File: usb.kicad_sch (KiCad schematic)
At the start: 1 part, among them U1 MIMX8MN5DVPIZAA

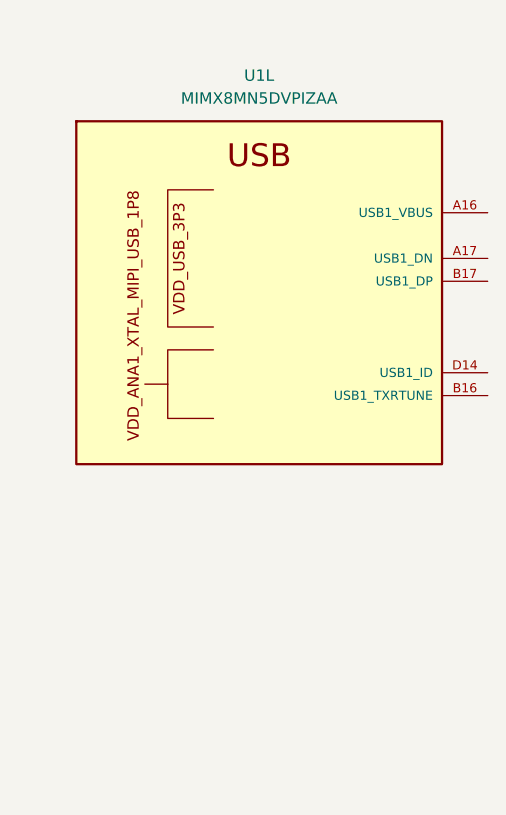
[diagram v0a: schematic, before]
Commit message: move to i.MX8M Mini
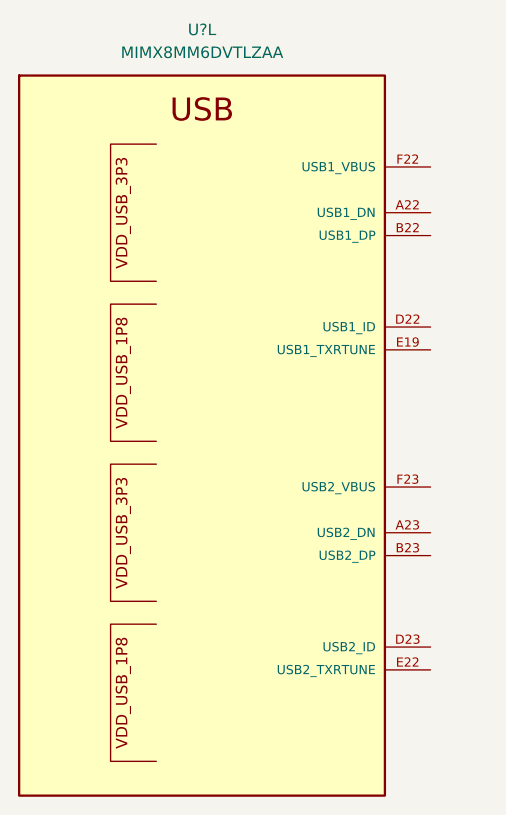
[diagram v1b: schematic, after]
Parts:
- removed U1: MIMX8MN5DVPIZAA, qsbc:SOT1967-1, symbol qsbc:MIMX8MN5DVPIZAA
- added U?: MIMX8MM6DVTLZAA, qsbc:SOT1967-1, symbol qsbc:MIMX8MM6DVTLZAA

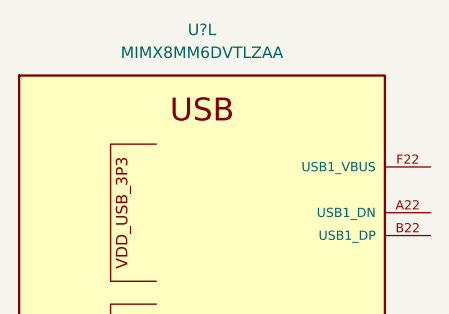
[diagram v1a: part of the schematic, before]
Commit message: ddr sch done
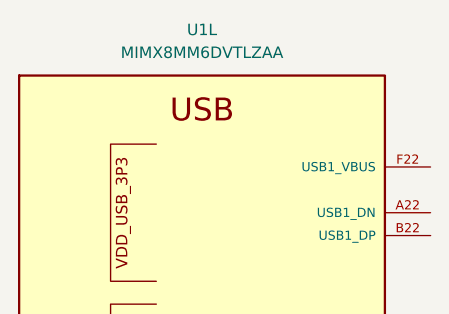
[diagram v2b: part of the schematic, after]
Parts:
- gave numbers to parts that had none: 1
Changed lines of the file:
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@@
   (symbol (lib_id "qsbc:MIMX8MM6DVTLZAA") (at 140.97 62.23 0) (unit 12)
     (in_bom yes) (on_board yes) (fields_autoplaced)
-    (property "Reference" "U?" (id 0) (at 140.97 43.18 0))
+    (property "Reference" "U1" (id 0) (at 140.97 43.18 0))
     (property "Value" "MIMX8MM6DVTLZAA" (id 1) (at 140.97 45.72 0))
     (property "Footprint" "qsbc:SOT1967-1" (id 2) (at 144.78 252.73 0)

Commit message: misc work, usb sch done
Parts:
- added C50, C51, C53, C? (x5): 0.1uF, Capacitor_SMD:C_0402_1005Metric, symbol Device:C
- added C52, C?: 1nF, Capacitor_SMD:C_0603_1608Metric, symbol Device:C
- added C54, C?: 10uF, Capacitor_SMD:C_0603_1608Metric, symbol Device:C
- added C? (x2): 0.22uF, Capacitor_SMD:C_0402_1005Metric, symbol Device:C
- added C?: 1uF, Capacitor_SMD:C_0402_1005Metric, symbol Device:C
- added D1: LED YELLOW, LED_SMD:LED_0402_1005Metric, symbol Device:LED
- added FB1, FB? (x3): FerriteBead, Resistor_SMD:R_0603_1608Metric, symbol Device:FerriteBead
- added J1, J3, J? (x2): USB_C_Receptacle_USB2.0, Connector_USB:USB_C_Receptacle_HRO_TYPE-C-31-M-12, symbol Connector:USB_C_Receptacle_USB2.0
- added R12, R13, R14, R? (x4): 100K, Resistor_SMD:R_0402_1005Metric, symbol Device:R
- added R15, R16, R? (x2): 0R, symbol Device:R
- added R17, R?: 30K, Resistor_SMD:R_0402_1005Metric, symbol Device:R
- added R18, R?: 1M, Resistor_SMD:R_0402_1005Metric, symbol Device:R
- added R? (x2): 30K, Resistor_SMD:R_0201_0603Metric, symbol Device:R
- added R? (x4): 0R, Resistor_SMD:R_0402_1005Metric, symbol Device:R
- added R?: 2.2K, Resistor_SMD:R_0402_1005Metric, symbol Device:R
- added R? (x4): 5.1K, Resistor_SMD:R_0402_1005Metric, symbol Device:R
- added R? (x2): 200R, Resistor_SMD:R_0201_0603Metric, symbol Device:R
- added R?: 10K, Resistor_SMD:R_0402_1005Metric, symbol Device:R
- added R?: 10m, Resistor_SMD:R_1206_3216Metric, symbol Device:R
- added TP?: TestPoint, TestPoint:TestPoint_Pad_D1.5mm, symbol Connector:TestPoint
- added U10, U?: TUSB320LI, Package_DFN_QFN:Texas_X2QFN-12_1.6x1.6mm_P0.4mm, symbol Interface_USB:TUSB320
- added U12, U4, U?: TPD4EUSB30, Package_SON:USON-10_2.5x1.0mm_P0.5mm, symbol qsbc:TPD4EUSB30
- added U19, U?: NX5P3363, Package_CSP:WLCSP-16_2.225x2.17mm_P0.5mm, symbol qsbc:NX5P3363
- added U20, U? (x3): D5V0H1B2LP, symbol qsbc:D5V0H1B2LP
- added U8, U?: 74LVC1G04, Package_TO_SOT_SMD:SOT-23-5, symbol 74xGxx:74LVC1G04
- added U?: INA231, qsbc:DSBGA-12, symbol qsbc:INA231
- added U?: CH343P, Package_DFN_QFN:QFN-16-1EP_3x3mm_P0.5mm_EP1.45x1.45mm_ThermalVias, symbol qsbc:CH343P
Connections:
- net USB1_DN: now reaches U1.A22 (USB1_DN)
- net USB1_DN: now also J?.A7 (D-), J?.B7 (D-), U?.4 (D2+), U?.7
- net USB2_DN: now reaches U1.A23 (USB2_DN)
- net USB2_DN: now also J3.A7 (D-), J3.B7 (D-), U12.4 (D2+), U12.7
- net USB1_DP: now reaches U1.B22 (USB1_DP)
- net USB1_DP: now also J?.A6 (D+), J?.B6 (D+), U?.5 (D2-), U?.6
- net USB2_DP: now reaches U1.B23 (USB2_DP)
- net USB2_DP: now also J3.A6 (D+), J3.B6 (D+), U12.5 (D2-), U12.6
- net USB1_ID: now reaches U1.D22 (USB1_ID)
- net USB1_ID: now also R?.2, U?.2, U?.9 (ID)
- net USB2_ID: now reaches U1.D23 (USB2_ID)
- net USB2_ID: now also R12.2, U10.9 (ID), U8.2
- net at U1.E19 (USB1_TXRTUNE): now also R?.1
- net at U1.E22 (USB2_TXRTUNE): now also R?.1
- net at U1.F22 (USB1_VBUS): now also R?.1
- net at U1.F23 (USB2_VBUS): now also R?.1
- new net: R?.1, U?.4
- new net: C?.1, U?.D4 (CAP)
- new net: FB?.1, J?.S1 (SHIELD) (x2)
- new net: R18.1, U10.4 (VBUS_DET)
- new net: FB1.1, J3.S1 (SHIELD)
- new net: R?.2, U?.13 (UART_RTS)
- new net: D1.2 (A), R?.1
- new net: R?.2, U?.12 (UART_DTR/TNOW)
- new net: R?.2, U?.15 (UART_CTS)
- new net: R?.2, U?.4 (UART_TXD)
- new net: R?.1, U?.4 (VBUS_DET)
- new net: R?.1, U?.A3 (ILIM)
- new net: R16.1, U8.4
- new net: C52.1, U19.D4 (CAP)
- new net: R?.1, U?.10 (~{ACT})
- new net: R?.2, U?.5 (UART_RXD)
- new net: R17.1, U19.A3 (ILIM)
- new net: U4.1 (D1+), U4.10
- new net: U4.2 (D1-), U4.9
- new net: FB?.1, J1.S1 (SHIELD)
- new net GND: C50.2, C51.2, C52.2, C53.2, C54.2, C?.2, C?.2, C?.2, C?.2, C?.2, C?.2, C?.2, C?.2, C?.2, C?.2, D1.1 (K), FB1.2, FB?.2, FB?.2, FB?.2, J1.A1 (GND), J1.A12 (GND), J1.B1 (GND), J1.B12 (GND), J3.A1 (GND), J3.A12 (GND), J3.B1 (GND), J3.B12 (GND), J?.A1 (GND), J?.A1 (GND), J?.A12 (GND), J?.A12 (GND), J?.B1 (GND), J?.B1 (GND), J?.B12 (GND), J?.B12 (GND), R17.2, R?.2, R?.2, R?.2, R?.2, R?.2, R?.2, R?.2, R?.2, U10.10 (GND), U10.11 (~{EN}), U10.5 (ADDR), U12.3 (GND), U12.8 (GND), U19.B3 (GND), U19.C3 (GND), U19.D3 (GND), U20.2, U4.3 (GND), U4.8 (GND), U8.3 (GND), U?.1 (VDDIO), U?.10 (GND), U?.11 (~{EN}), U?.2, U?.2, U?.2, U?.2 (GND), U?.3 (GND), U?.3 (GND), U?.8 (GND), U?.B3 (A0), U?.B3 (GND), U?.C1 (GND), U?.C3 (A1), U?.C3 (GND), U?.D3 (GND)
- new net I2Cx_SCL: U10.8 (SCL/OUT2), U?.8 (SCL/OUT2), U?.A1 (SCL)
- new net I2Cx_SDA: U10.7 (SDA/OUT1), U?.7 (SDA/OUT1), U?.A2 (SDA)
- new net UART2_CTS: R?.1
- new net UART2_RTS: R?.1
- new net UART2_RXI: R?.1
- new net UART2_TXO: R?.1
- new net USB1_CC1: J?.A5 (CC1), U?.1 (CC1), U?.1 (D1+), U?.10
- new net USB1_CC2: J?.B5 (CC2), U?.2 (CC2), U?.2 (D1-), U?.9
- new net USB1_VBUS: C?.1, C?.1, J?.A4 (VBUS), J?.A9 (VBUS), J?.B4 (VBUS), J?.B9 (VBUS), R?.2, R?.2, U?.1, U?.C2 (VBUS), U?.D1 (VBUS), U?.D2 (VBUS)
- new net USB1_VBUS_EN: R?.1
- new net USB1_VBUS_EN_R: R?.2, R?.2, U?.B4 (EN)
- new net USB2_CC1: J3.A5 (CC1), U10.1 (CC1), U12.1 (D1+), U12.10
- new net USB2_CC2: J3.B5 (CC2), U10.2 (CC2), U12.2 (D1-), U12.9
- new net USB2_VBUS: C54.1, C?.1, J3.A4 (VBUS), J3.A9 (VBUS), J3.B4 (VBUS), J3.B9 (VBUS), R18.2, R?.2, U19.C2 (VBUS), U19.D1 (VBUS), U19.D2 (VBUS), U20.1
- new net USB2_VBUS_EN: R15.1
- new net USB2_VBUS_EN_R: R15.2, R16.2, U19.B4 (EN)
- new net USB3_CC1: J1.A5 (CC1), R?.1
- new net USB3_CC2: J1.B5 (CC2), R?.1
- new net USB3_DN: J1.A7 (D-), J1.B7 (D-), U4.5 (D2-), U4.6, U?.8 (USB_DN)
- new net USB3_DP: J1.A6 (D+), J1.B6 (D+), U4.4 (D2+), U4.7, U?.7 (USB_DP)
- new net USB3_VBUS: J1.A4 (VBUS), J1.A9 (VBUS), J1.B4 (VBUS), J1.B9 (VBUS), U?.1, U?.9 (USB_VBUS)
- new net USB4_CC1: J?.A5 (CC1), R?.1
- new net USB4_CC2: J?.B5 (CC2), R?.1
- new net USB4_VBUS: J?.A4 (VBUS), J?.A9 (VBUS), J?.B4 (VBUS), J?.B9 (VBUS), R?.1, TP?.1, U?.1, U?.D1 (Vbus), U?.D3 (Vin+)
- new net VCC: C51.1, C?.1, C?.1, R12.1, R13.1, R14.1, R?.1, R?.1, R?.1, R?.1, U8.5 (VCC), U?.1 (VDDIO), U?.5 (VCC)
- new net VDD_3.3V: C53.1, C?.1, C?.1, C?.1, U10.12 (VDD), U?.12 (VDD), U?.3 (VDD5), U?.5 (ADDR), U?.6 (V3), U?.B1 (VS)
- new net VSYS_5V: C50.1, C?.1, R?.2, U19.A1 (VIN), U19.A2 (VIN), U?.A1 (VIN), U?.A2 (VIN), U?.D2 (Vin-)
- new net ~{INA_ALERT}: R?.2, U?.A3 (~{Alert})
- new net ~{USB1_INT}: R?.2, U?.6 (~{INT}/OUT3)
- new net ~{USB1_VBUS_FLT}: R?.2, U?.A4 (~{FLT})
- new net ~{USB2_INT}: R14.2, U10.6 (~{INT}/OUT3)
- new net ~{USB2_VBUS_FLT}: R13.2, U19.A4 (~{FLT})
- no-connect marks 0 -> 27
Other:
- note added: "1.6A Current Limit"
- note added: "I2C Addr: 0x47"
- note added: "I2C Addr: 0x67"
- note added: "I2C Address: 0x40"
- note added: "Place for Adaptive Baud Rate"
- moved on the sheet: U1L

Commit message: enet sch done, other misc sch work
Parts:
- gave numbers to parts that had none: 48
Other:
- moved on the sheet: C64

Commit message: pcie done, misc fixes for usb, enet
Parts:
- added C?: 0.1uF, Capacitor_SMD:C_0402_1005Metric, symbol Device:C
- added R?: 10K, Resistor_SMD:R_0402_1005Metric, symbol Device:R
- added U?: TS3USB221E, Package_DFN_QFN:Texas_R-PUQFN-N10, symbol qsbc:TS3USB221E
- added U?: TPD4EUSB30, Package_SON:USON-10_2.5x1.0mm_P0.5mm, symbol qsbc:TPD4EUSB30
- C51, C56: DNP (none) -> DNP
- U10, U6: value TUSB320LI -> TUSB320LAI
- U2, U8: footprint Package_TO_SOT_SMD:SOT-23-5 -> Package_TO_SOT_SMD:SOT-553; DNP (none) -> DNP
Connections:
- net GND: now also C?.2, R?.2, U?.3 (GND), U?.5 (GND), U?.6 (~{OE}), U?.8 (GND)
- net USB3_DN: now also U?.4 (2D-); no longer U11.8 (USB_DN)
- net USB3_DP: now also U?.3 (2D+); no longer U11.7 (USB_DP)
- net USB3_VBUS: now also R?.1, U?.9 (S); no longer U11.9 (USB_VBUS)
- net VDD_3.3V: now also U11.9 (USB_VBUS), C?.1, U?.10 (VCC)
- net USB4_DP: now reaches J7.A6 (D+)
- net USB4_DP: now also J7.B6 (D+), U?.1 (1D+), U?.4 (D2+), U?.7
- net USB4_DN: now reaches J7.A7 (D-)
- net USB4_DN: now also J7.B7 (D-), U?.2 (1D-), U?.5 (D2-), U?.6
- new net: U?.1 (D1+), U?.10
- new net: U?.2 (D1-), U?.9
- new net USBUART_DN: U11.8 (USB_DN), U?.7 (D-)
- new net USBUART_DP: U11.7 (USB_DP), U?.8 (D+)
- no-connect marks 27 -> 25
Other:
- moved on the sheet: FB3, J1, R38, R40, U22, U4

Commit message: storage done, peri work, misc fixes
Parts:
- removed D1: LED YELLOW, LED_SMD:LED_0402_1005Metric, symbol Device:LED
- removed R34: 2.2K, Resistor_SMD:R_0402_1005Metric, symbol Device:R
- added C? (x2): 0.1uF, Capacitor_SMD:C_0402_1005Metric, symbol Device:C
- added D?: LED_Orange, LED_SMD:LED_0603_1608Metric, symbol Device:LED
- added D?: LED_Yellow, LED_SMD:LED_0603_1608Metric, symbol Device:LED
- added R? (x2): 2.2K, Resistor_SMD:R_0402_1005Metric, symbol Device:R
- added U? (x2): 74LVC1G07, symbol 74xGxx:74LVC1G07
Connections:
- net GND: now also C?.2, C?.2, U?.3 (GND), U?.3 (GND)
- net VCC: now also C?.1, C?.1, U?.5 (VCC), U?.5 (VCC)
- net VDD_3.3V: now also R?.1, R?.1
- net at R30.2, U11.4 (UART_TXD): now also U?.2
- net at R31.2, U11.5 (UART_RXD): now also U?.2
- net I2Cx_SCL renamed I2C4_SCL
- net I2Cx_SDA renamed I2C4_SDA
- new net: D?.1 (K), U?.4 (x2)
- new net: D?.2 (A), R?.2 (x2)
- no-connect marks 25 -> 26
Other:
- moved on the sheet: C62, C63, C?, FB3, J1, R30, R31, R32, R33, R36, R38, R40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

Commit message: ddr: add dual die support, misc work
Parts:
- C128, C129, C130: renamed from C?; Rating 6.3V/20% -> 25V/20%
- C50, C55, C63: Rating 10V/20% -> 25V/20%
- C51, C53, C56, C58, C64: Rating 6.3V/20% -> 25V/20%
- C60, C61: footprint Capacitor_SMD:C_0402_1005Metric -> Capacitor_SMD:C_0201_0603Metric
- R12, R13, R14, R19, R20, R21, R35: Rating 50mW/5% -> 50mW/1%
- R15, R16, R22, R23: footprint (none) -> Resistor_SMD:R_0402_1005Metric
- R17, R24: footprint Resistor_SMD:R_0402_1005Metric -> Resistor_SMD:R_0201_0603Metric
- R71: renamed from R?; Rating 50mW/5% -> 50mW/1%
- U2, U8: footprint Package_TO_SOT_SMD:SOT-553 -> Package_TO_SOT_SMD:SOT-23-5
- U20, U22, U23, U7: footprint (none) -> qsbc:DFN100X60X45-2N
- U26, U27: renamed from U?; footprint (none) -> Package_TO_SOT_SMD:SOT-23-5
- gave numbers to parts that had none: 6
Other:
- company: (none) -> Q-LAB
- title: (none) -> QSBC

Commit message: fix ref desgigators, add table for dram config
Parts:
- renumbered C55 to C107, C50 to C108, C56 to C109, C51 to C110, C57 to C111, C52 to C112, C58 to C113, C53 to C114, C59 to C115, C54 to C116, C60 to C117, C61 to C118, C128 to C119, C129 to C120, C62 to C121, C63 to C122, C64 to C123, C130 to C124, FB2 to FB1, FB1 to FB2, J2 to J1, J3 to J2, J1 to J3, J7 to J4, R12 to R20, R20 to R21, R21 to R22, R13 to R23, R14 to R24, R22 to R25, R15 to R26, R23 to R27, R16 to R28, R24 to R29, R17 to R30, R25 to R31, R18 to R32, R26 to R33, R27 to R34, R28 to R35, R29 to R36, R30 to R37, R31 to R38, R32 to R39, R33 to R40, R35 to R41, R38 to R42, R34 to R43, R40 to R44, R36 to R45, R70 to R46, R37 to R47, R71 to R48, R39 to R49, R41 to R50, TP21 to TP23, U7 to U10, U20 to U11, U9 to U12, U12 to U13, U26 to U14, U27 to U15, U22 to U16, U11 to U17, U4 to U18, U21 to U19, U23 to U20, U28 to U21, U29 to U22, U2 to U4, U8 to U5, U5 to U6, U6 to U7, U19 to U8, U10 to U9
